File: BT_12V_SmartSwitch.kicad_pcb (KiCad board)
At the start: 2 copper layers, 41 x 28 mm, 43 parts, among them J1 Screw_Terminal_01x02, J2 Conn_02x03_Odd_Even, J3 Conn_02x02_Odd_Even, J4 Conn_02x03_Odd_Even, Q1 PZT2222A, Q2 PZT2222A, Q3 IRLML6402, Q4 IRLML6402, Q5 IRLML6402, Q6 PZT2222A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

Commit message: RevA Layout complete pending last checks
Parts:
- added J5: Conn_01x02_Female, Connector_PinSocket_2.54mm:PinSocket_1x02_P2.54mm_Vertical, F.Cu at (172.5, 40.0)
- added R12: 10k, Resistor_SMD:R_0805_2012Metric, F.Cu at (169.8, 40.5)
- moved C7 1.60 mm to (157.8, 63.8), turned to 90 degrees
- moved C4 1.52 mm to (175.8, 42.2)
- moved R10 1.03 mm to (159.8, 64.0), turned to 90 degrees
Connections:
- C2 pad 1: RESET -> VDD
- C3 pad 1: RESET -> VDD
- C4 pad 1: RESET -> VDD
- C5 pad 1: RESET -> VDD
- C6 pad 1: RESET -> VDD
- C7 pad 1: RESET -> VDD
- C7 pad 2: Net-(C7-Pad2) -> RESET
- J4 pad 2: RESET -> VDD
- R10 pad 1: RESET -> VDD
- R10 pad 2: Net-(C7-Pad2) -> RESET
- R5 pad 1: RESET -> VDD
- SW1 pad 2: Net-(C7-Pad2) -> RESET
- U1 pad 2: RESET -> VDD
- U2 pad 17: RESET -> VDD
- U2 pad 22: RESET -> VDD
- U2 pad 6: RESET -> VDD
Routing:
- net RESET: track 145.5 -> 38.2 mm, vias 8 -> 1
- net VDD: track 0.00 -> 102.0 mm, vias 0 -> 4
- net GND: track 45.3 -> 60.5 mm, vias 19 -> 18
- net GPIO_0: track 0.00 -> 13.5 mm
- net SPI_SSN: track 24.4 -> 30.1 mm, vias 0 -> 1
- net SPI_SCK: track 20.5 -> 17.2 mm, vias 0 -> 1
- net SPI_MOSI: track 18.1 -> 14.8 mm, vias 0 -> 1
- net CTRL_OUT4: track 33.0 -> 30.9 mm, vias 0 -> 2
- net +12V: track 34.0 -> 33.0 mm
- net SPI_MISO: track 23.2 -> 22.5 mm, vias 0 -> 1
- added copper zone on F.Cu, net VDD
- removed copper zone on F.Cu, net RESET
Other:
- board text added: "12V BT SmartSwitch Rev A 20190103"
- board text added: "SPI ICSP: 1 - MISO 2 - 3.3V+ 3 - SCK 4 - MOSI 5 - RST 6 - GND"
- board text removed: "SPI ICSP: 1 - MISO 2 - 3.3V+ 3 - SCK 4 - MOSI 5 - SSN 6 - GND"

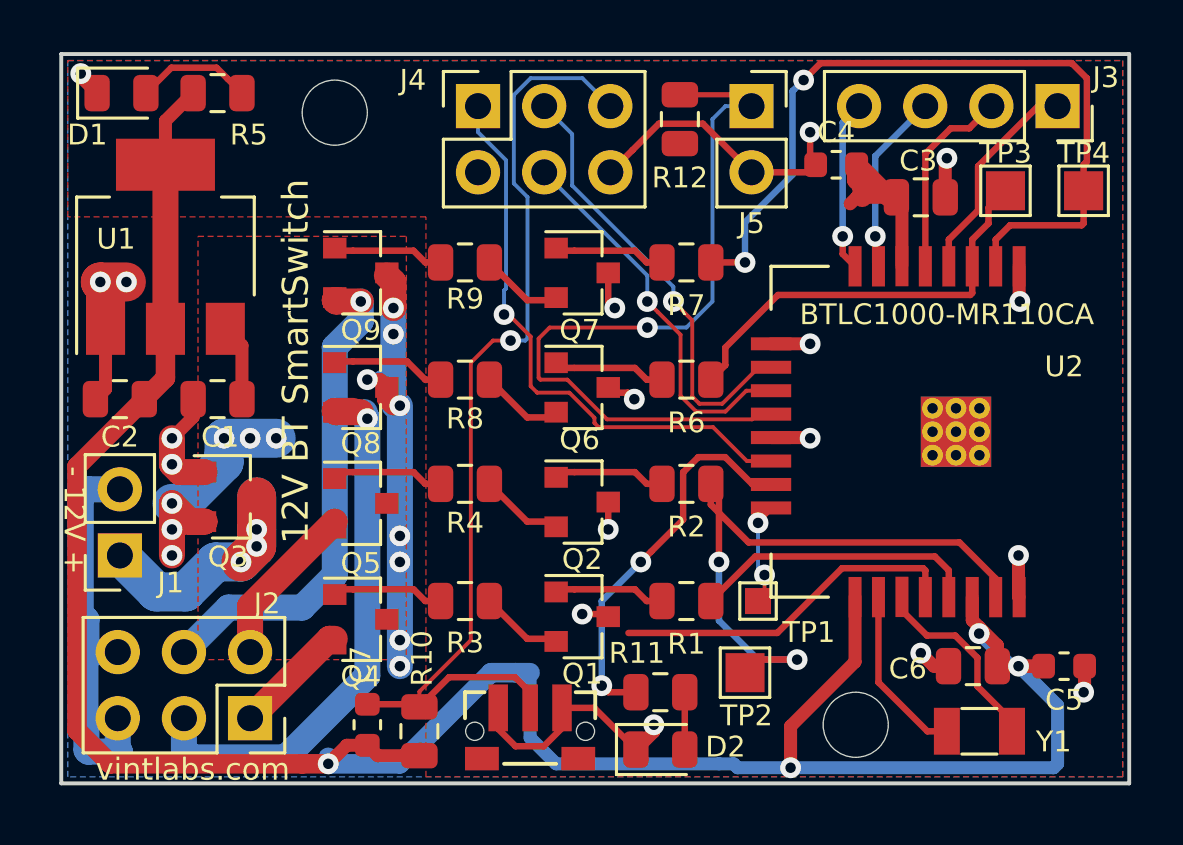
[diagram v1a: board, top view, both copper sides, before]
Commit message: Misc tidying up of traces and SS
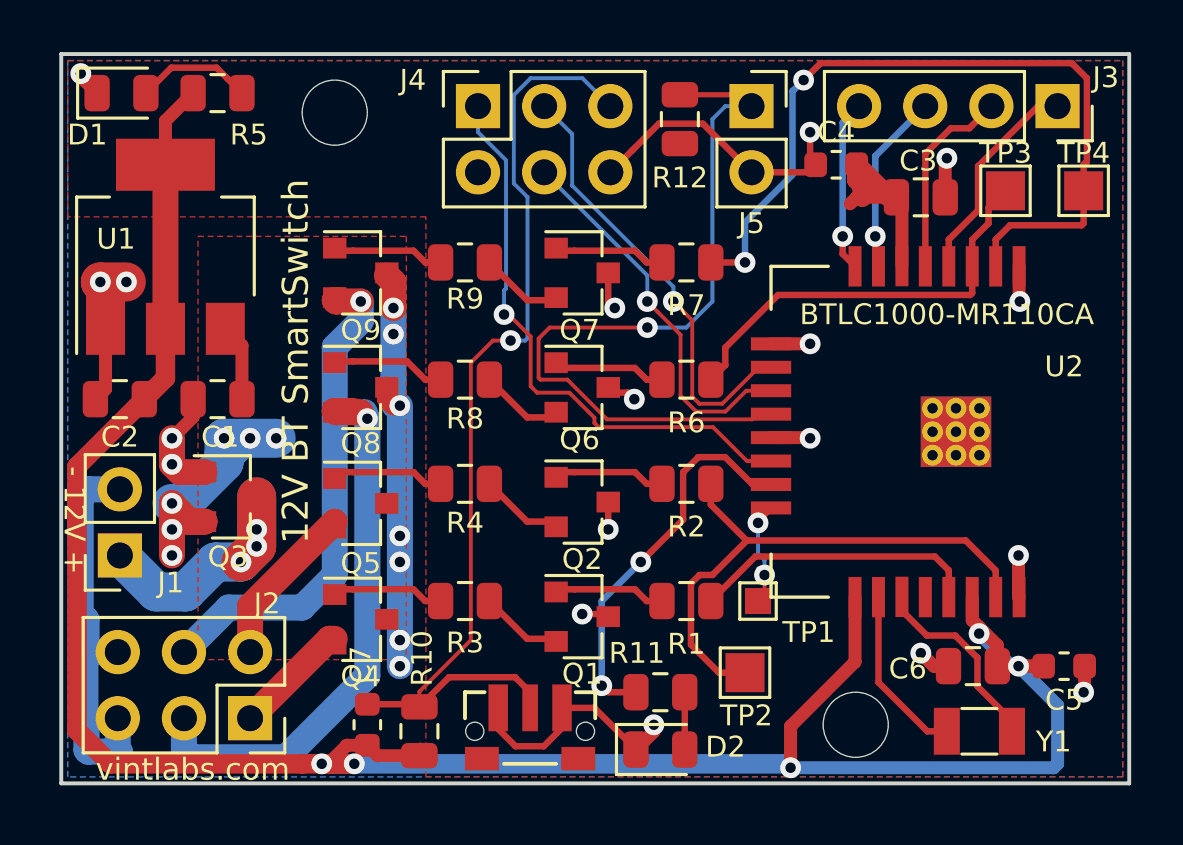
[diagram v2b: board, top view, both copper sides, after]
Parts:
- added REF**: OSHW-Logo_5.7x6mm_SilkScreen, Symbol:OSHW-Logo_5.7x6mm_SilkScreen, B.Cu at (150.8, 42.5)
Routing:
- net GPIO_0: track 13.5 -> 0.00 mm
- net VDD: track 102.0 -> 98.6 mm, vias 4 -> 5
- net CTRL_OUT2: track 24.8 -> 21.5 mm, vias 2 -> 0
- net +12V: track 33.0 -> 31.9 mm, vias 14 -> 13
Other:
- board text added: "5V-18V IN"
- board text added: "Input Connections: Red - +V in (5V-18V) Black - GND Output Connections: Green - OUT1 Blue - OUT2 Yellow - OUT3 White - OUT4"
- board text removed: "12V IN"
- board text removed: "Input Connections: Red - +12V in (18V MAX) Black - GND Output Connections: Green - OUT1 Blue - OUT2 Yellow - OUT3 White - OUT4"

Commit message: Couple more traces made prettier
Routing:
- net +12V: track 31.9 -> 32.9 mm
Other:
- board text added: "SPI ICSP: 1 - MISO 2 - +3.3V 3 - SCK 4 - MOSI 5 - RST 6 - GND"
- board text removed: "SPI ICSP: 1 - MISO 2 - 3.3V+ 3 - SCK 4 - MOSI 5 - RST 6 - GND"
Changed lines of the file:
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@@
     (thickness 1.6)
     (drawings 46)
-    (tracks 425)
+    (tracks 421)
     (zones 0)
     (modules 46)
@@
   )
   (setup
-    (last_trace_width 0.75)
+    (last_trace_width 1)
     (user_trace_width 0.15)
     (user_trace_width 0.2)
@@
     (effects (font (size 1 1) (thickness 0.15)) (justify mirror))
   )
-  (gr_text "SPI ICSP:\n1 - MISO\n2 - 3.3V+\n3 - SCK\n4 - MOSI\n5 - RST\n6 - GND" (at 182.25 50) (layer B.SilkS)
+  (gr_text "SPI ICSP:\n1 - MISO\n2 - +3.3V\n3 - SCK\n4 - MOSI\n5 - RST\n6 - GND" (at 182.25 50) (layer B.SilkS)
     (effects (font (size 1 1) (thickness 0.15)) (justify left mirror))
   )
@@
   (via (at 159 61.5) (size 0.8) (drill 0.4) (layers F.Cu B.Cu) (net 10))
   (via (at 159 51.5) (size 0.8) (drill 0.4) (layers F.Cu B.Cu) (net 10))
-  (via (at 158.75 48.75) (size 0.8) (drill 0.4) (layers F.Cu B.Cu) (net 10))
+  (via (at 159 48.75) (size 0.8) (drill 0.4) (layers F.Cu B.Cu) (net 10))
   (via (at 150.25 55.25) (size 0.8) (drill 0.4) (layers F.Cu B.Cu) (net 10))
   (via (at 150.25 56.25) (size 0.8) (drill 0.4) (layers F.Cu B.Cu) (net 10))
@@
   (segment (start 158.5 51.25) (end 158.75 51.5) (width 0.75) (layer F.Cu) (net 10))
   (segment (start 158.5 50.75) (end 158.5 51.25) (width 0.75) (layer F.Cu) (net 10))
-  (segment (start 158.75 51.5) (end 158.75 51) (width 0.75) (layer B.Cu) (net 10))
-  (segment (start 158.75 51.5) (end 158.75 50.934315) (width 0.75) (layer B.Cu) (net 10))
-  (via (at 158.75 47.75) (size 0.8) (drill 0.4) (layers F.Cu B.Cu) (net 10))
+  (via (at 159 47.75) (size 0.8) (drill 0.4) (layers F.Cu B.Cu) (net 10))
   (segment (start 158.75 46.75) (end 158.75 47.75) (width 1) (layer F.Cu) (net 10))
   (segment (start 158.5 46.5) (end 158.75 46.75) (width 1) (layer F.Cu) (net 10))
-  (segment (start 158.80002 51.273651) (end 158.80002 51.5) (width 1) (layer B.Cu) (net 10))
-  (segment (start 158.75 51.223631) (end 158.80002 51.273651) (width 1) (layer B.Cu) (net 10))
   (via (at 159 56.5) (size 0.8) (drill 0.4) (layers F.Cu B.Cu) (net 10))
   (via (at 159 57.5) (size 0.8) (drill 0.4) (layers F.Cu B.Cu) (net 10))
   (via (at 159 60.5) (size 0.8) (drill 0.4) (layers F.Cu B.Cu) (net 10))
   (segment (start 159 51.5) (end 159 61.5) (width 1) (layer B.Cu) (net 10))
-  (segment (start 158.75 47.75) (end 158.75 50.5) (width 1) (layer B.Cu) (net 10))
-  (segment (start 158.75 50.5) (end 158.75 51.223631) (width 1) (layer B.Cu) (net 10))
   (segment (start 179.25 64) (end 180 64) (width 0.25) (layer F.Cu) (net 11))
   (segment (start 177.374 62.124) (end 179.25 64) (width 0.25) (layer F.Cu) (net 11))
@@
   (segment (start 156.55 51.75) (end 156.5 51.7) (width 1) (layer F.Cu) (net 34))
   (segment (start 157.5 51.75) (end 156.55 51.75) (width 1) (layer F.Cu) (net 34))
-  (segment (start 157.65001 51.90001) (end 157.65001 51.75) (width 1) (layer B.Cu) (net 34))
   (segment (start 150.71 63.5) (end 150.71 64.702081) (width 1) (layer B.Cu) (net 34))
   (segment (start 157.75 61.870002) (end 157.75 52) (width 1) (layer B.Cu) (net 34))
@@
   (segment (start 151.00792 65.000001) (end 154.620001 65.000001) (width 1) (layer B.Cu) (net 34))
   (segment (start 154.620001 65.000001) (end 157.75 61.870002) (width 1) (layer B.Cu) (net 34))
-  (segment (start 157.75 52) (end 157.65001 51.90001) (width 1) (layer B.Cu) (net 34))
   (via (at 157.5 47.5) (size 0.8) (drill 0.4) (layers F.Cu B.Cu) (net 35))
   (segment (start 156.5 47.45) (end 156.7 47.45) (width 1) (layer F.Cu) (net 35))
@@
   (segment (start 152.325998 53.674002) (end 152.25 53.674002) (width 1) (layer B.Cu) (net 10))
   (segment (start 153.25 52.75) (end 152.325998 53.674002) (width 1) (layer B.Cu) (net 10))
+  (segment (start 159 47) (end 158.75 46.75) (width 1) (layer F.Cu) (net 10))
+  (segment (start 159 47.75) (end 159 47) (width 1) (layer F.Cu) (net 10))
+  (segment (start 159 47.75) (end 159 48.75) (width 1) (layer F.Cu) (net 10))
+  (segment (start 159 51.5) (end 159 47.75) (width 1) (layer B.Cu) (net 10))
   (segment (start 170.9375 55.3) (end 170.9375 54.5) (width 0.25) (layer F.Cu) (net 31))
   (segment (start 181.874 57.825) (end 180.724001 56.675001) (width 0.25) (layer F.Cu) (net 31))
@@
       )
     )
+  )
+  (zone (net 0) (net_name "") (layer B.Cu) (hatch edge 0.508)
+    (connect_pads (clearance 0.508))
+    (min_thickness 0.254)
+    (keepout (tracks allowed) (vias allowed) (copperpour not_allowed))
+    (fill (arc_segments 16) (thermal_gap 0.508) (thermal_bridge_width 0.508))
+    (polygon
+      (pts
+        (xy 160.25 46.25) (xy 160.25 65.5) (xy 155.5 65.5) (xy 155.5 46.25)
+      )
+    )
